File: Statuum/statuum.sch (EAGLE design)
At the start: 73 parts, among them IC1 LM317MABT, J1 POWER_JACKPTH, J2 NRJ3HF-1, J3 RCJ-21XXMILL, Q1 2N5484, Q10 ZVN4306A, Q11 ZVN4306A, Q12 ZVN4306A, Q2 2N5484, Q3 ZVN4306A, Q4 ZVN4306A, Q5 ZVN4306A, Q6 ZVN4306A, Q7 2N5484, Q8 2N5484, Q9 ZVN4306A

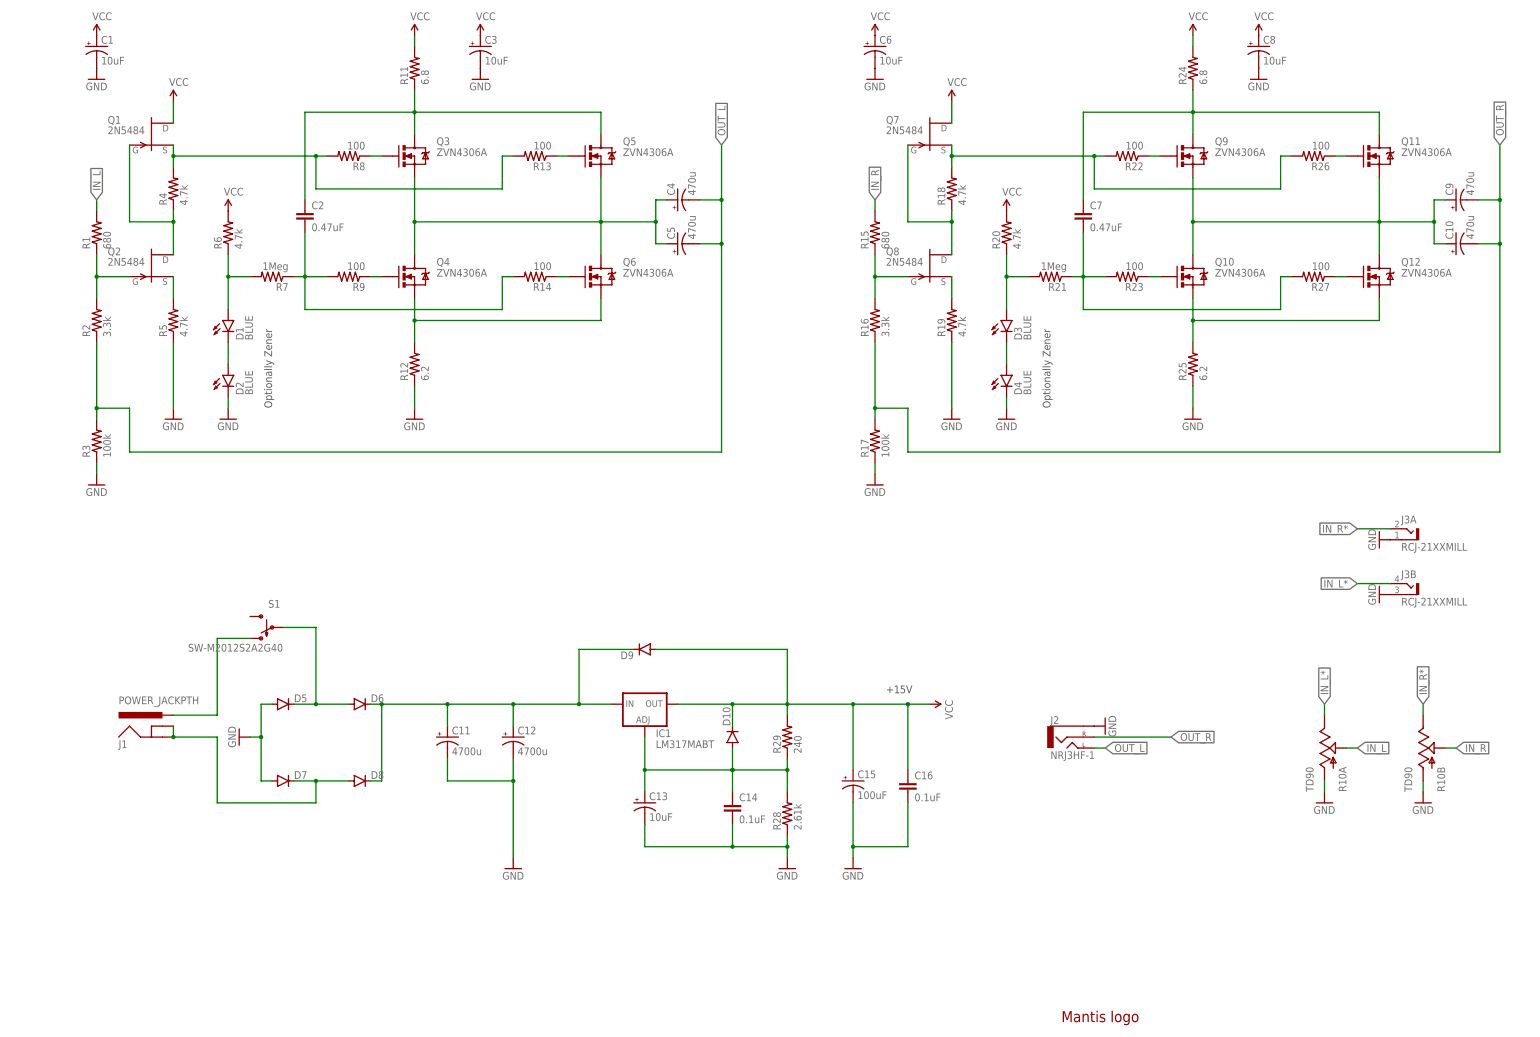
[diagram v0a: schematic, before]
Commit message: Desktop version changed to IRF510 output
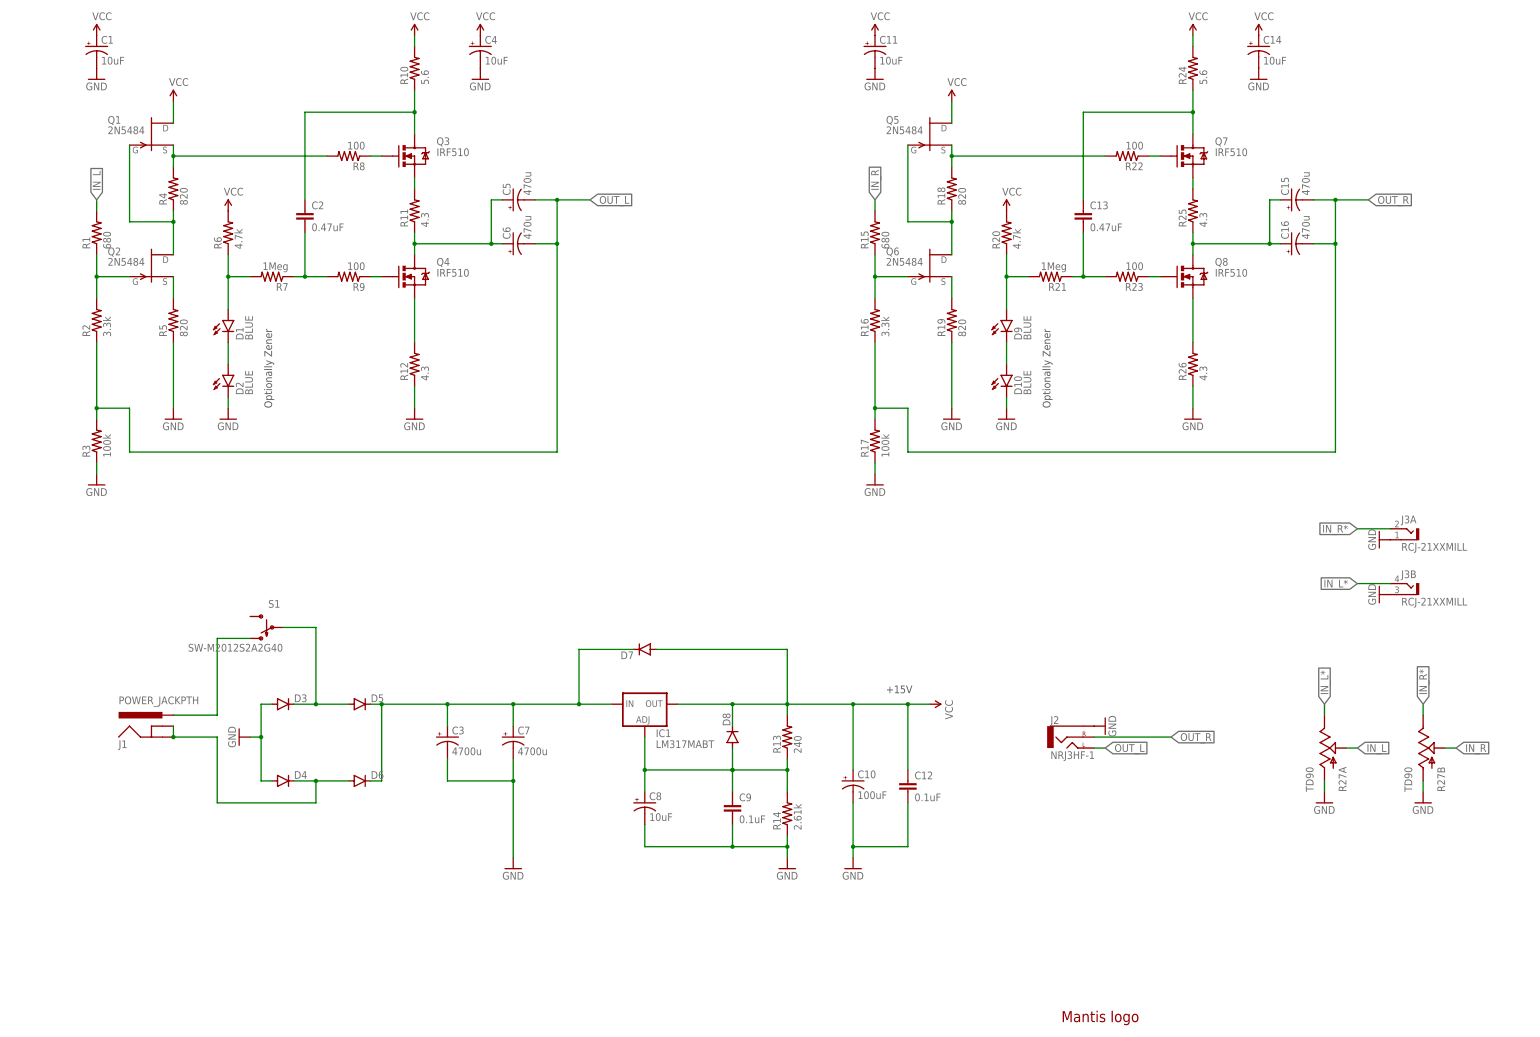
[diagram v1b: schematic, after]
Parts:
- removed Q10, Q11, Q12, Q9: ZVN4306A, my-tran:ZVN4306A
- removed R28: 2.61k, my-res:RESISTORPTH-1/4W
- removed R29: 240, my-res:RESISTORPTH-1/4W
- C10: value 470u -> 100uF
- C11: value 4700u -> 10uF; device SparkFun-Capacitors:CAP_POLPTH3 -> my-cap:CAP_POLPTH1-SM
- C12: value 4700u -> 0.1uF; device SparkFun-Capacitors:CAP_POLPTH3 -> SparkFun-Capacitors:CAPPTH
- C13: value 10uF -> 0.47uF; device my-cap:CAP_POLPTH1-SM -> capacitor-wima:C5/3.5
- C14: value 0.1uF -> 10uF; device SparkFun-Capacitors:CAPPTH -> my-cap:CAP_POLPTH1-SM
- C15: value 100uF -> 470u
- C16: value 0.1uF -> 470u; device SparkFun-Capacitors:CAPPTH -> my-cap:CAP_POLPTH8MM
- C3: value 10uF -> 4700u; device my-cap:CAP_POLPTH1-SM -> SparkFun-Capacitors:CAP_POLPTH3
- C4: value 470u -> 10uF; device my-cap:CAP_POLPTH8MM -> my-cap:CAP_POLPTH1-SM
- C6: value 10uF -> 470u; device my-cap:CAP_POLPTH1-SM -> my-cap:CAP_POLPTH8MM
- C7: value 0.47uF -> 4700u; device capacitor-wima:C5/3.5 -> SparkFun-Capacitors:CAP_POLPTH3
- C9: value 470u -> 0.1uF; device my-cap:CAP_POLPTH8MM -> SparkFun-Capacitors:CAPPTH
- D10, D9: value (none) -> BLUE; device SparkFun-DiscreteSemi:DIODEPTH -> my:LED3MM-SM
- D3, D4: value BLUE -> (none); device my:LED3MM-SM -> SparkFun-DiscreteSemi:DIODEPTH
- Q3, Q4: value ZVN4306A -> IRF510; device my-tran:ZVN4306A -> my-tran:IRF510
- Q5, Q6: value ZVN4306A -> 2N5484; device my-tran:ZVN4306A -> my-tran:2N5484
- Q7, Q8: value 2N5484 -> IRF510; device my-tran:2N5484 -> my-tran:IRF510
- R10: value TD90 -> 5.6; device my:TD90 -> my-res:RESISTORPTH-1/4W
- R11: value 6.8 -> 4.3
- R12, R25: value 6.2 -> 4.3
- R13: value 100 -> 240
- R14: value 100 -> 2.61k
- R18, R19, R4, R5: value 4.7k -> 820
- R24: value 6.8 -> 5.6
- R26: value 100 -> 4.3
- R27: value 100 -> TD90; device my-res:RESISTORPTH-1/4W -> my:TD90
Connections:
- removed net N$26: Q11.G, R26.1
- removed net N$27: Q12.G, R27.1
- net GND: now also C10.-, C12.2, C14.-, C4.-, C7.-, C9.2, D10.C, D3.A, D4.A, R14.1, R26.1, R27A.A, R27B.A; no longer C12.-, C13.-, C14.2, C15.-, C16.2, C6.-, D4.C, D5.A, D7.A, R10A.A, R10B.A, R25.1, R28.1
- net IN_L: now also R27A.S; no longer R10A.S
- net IN_L*: now also R27A.E; no longer R10A.E
- net IN_R: now also R27B.S; no longer R10B.S
- net IN_R*: now also R27B.E; no longer R10B.E
- net N$1: no longer R13.2
- net N$10: no longer Q6.S
- net N$11: now also R10.1; no longer Q5.D, R11.1
- net N$12: now also C6.+, R11.1; no longer C4.+, Q3.S, Q5.S, Q6.D
- net N$13: now also D3.C, D5.A; no longer D5.C, D6.A
- net N$15: no longer R14.2
- net N$16: now also Q5.S; no longer Q7.S, R26.2
- net N$17: now also Q5.G, Q6.D; no longer Q7.G, Q8.D
- net N$18: now also Q6.S; no longer Q8.S
- net N$19: now also Q6.G; no longer Q8.G
- net N$20: now also Q7.G; no longer Q9.G
- net N$21: now also Q8.G; no longer Q10.G
- net N$22: now also Q8.S, R26.2; no longer Q10.S, Q12.S, R25.2
- net N$23: now also C13.1, Q7.D; no longer C7.1, Q11.D, Q9.D
- net N$24: now also D9.A; no longer D3.A
- net N$25: now also D10.A, D9.C; no longer D3.C, D4.A
- net N$28: now also C13.2; no longer C7.2, R27.2
- net N$29: now also C15.+, C16.+, Q8.D, R25.1; no longer C10.+, C9.+, Q10.D, Q11.S, Q12.D, Q9.S
- net N$30: now also D4.C, D6.A; no longer D7.C, D8.A
- net N$32: now also C8.+, C9.1, D8.A, R13.1, R14.2; no longer C13.+, C14.1, D10.A, R28.2, R29.1
- net N$33: now also C3.+, C7.+, D5.C, D7.C; no longer C11.+, C12.+, D8.C, D9.C
- net N$7: now also Q3.S, R11.2; no longer Q5.G, R13.1
- net N$9: now also Q7.S, R25.2; no longer Q6.G, R14.1
- net OUT_L: now also C6.-; no longer C4.-
- net OUT_R: now also C15.-, C16.-; no longer C10.-, C9.-
- net VCC: now also C10.+, C11.+, C12.1, C14.+, C4.+, D7.A, D8.C, Q5.D, R10.2, R13.2; no longer C15.+, C16.1, C3.+, C6.+, C8.+, D10.C, D9.A, Q7.D, R11.2, R29.2
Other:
- moved on the sheet: C10, C11, C15, C3, C4, C5, C6, C8, D5, D6, D7, D8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

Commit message: Mounting holes
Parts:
- added H1: MOUNT-PAD-ROUND3.2, holes:MOUNT-PAD-ROUND3.2
- added H2: MOUNT-HOLE3.2, holes:MOUNT-HOLE3.2
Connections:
- net GND: now also H1.MOUNT
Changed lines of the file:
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@@
 <part name="Q8" library="my-tran" deviceset="IRF510" device=""/>
 <part name="R25" library="my-res" deviceset="RESISTOR" device="PTH-1/4W" value="4.3"/>
+<part name="H1" library="holes" deviceset="MOUNT-PAD-ROUND" device="3.2"/>
+<part name="H2" library="holes" deviceset="MOUNT-HOLE" device="3.2"/>
+<part name="GND22" library="SparkFun-Aesthetics" deviceset="GND" device=""/>
 </parts>
 <sheets>
@@
 <instance part="Q8" gate="G$1" x="287.02" y="180.34"/>
 <instance part="R25" gate="G$1" x="287.02" y="195.58" rot="R90"/>
+<instance part="H1" gate="G$1" x="294.64" y="35.56"/>
+<instance part="H2" gate="G$1" x="340.36" y="35.56"/>
+<instance part="GND22" gate="1" x="287.02" y="35.56" rot="R270"/>
 </instances>
 <busses>
@@
 <junction x="208.28" y="48.26"/>
 </segment>
-</net>
+<segment>
+<pinref part="H1" gate="G$1" pin="MOUNT"/>
+<wire x1="292.1" y1="35.56" x2="289.56" y2="35.56" width="0.1524" layer="91"/>
+<pinref part="GND22" gate="1" pin="GND"/>
+</segment>
+</net>

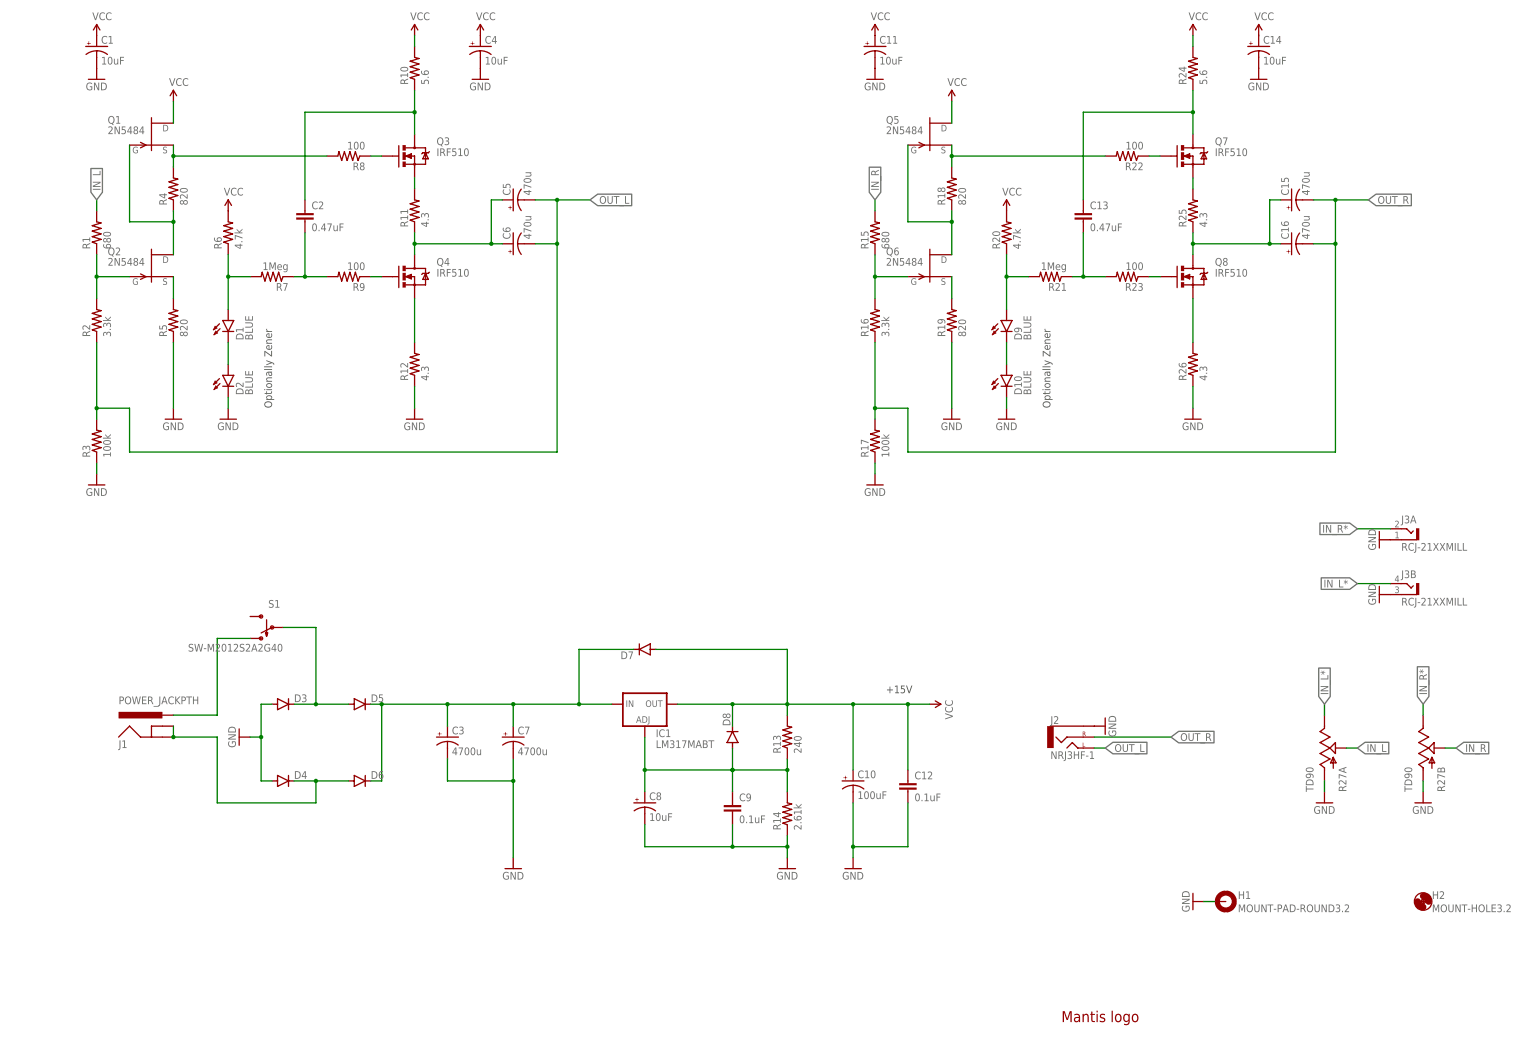
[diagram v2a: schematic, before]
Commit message: VBE multiplier added
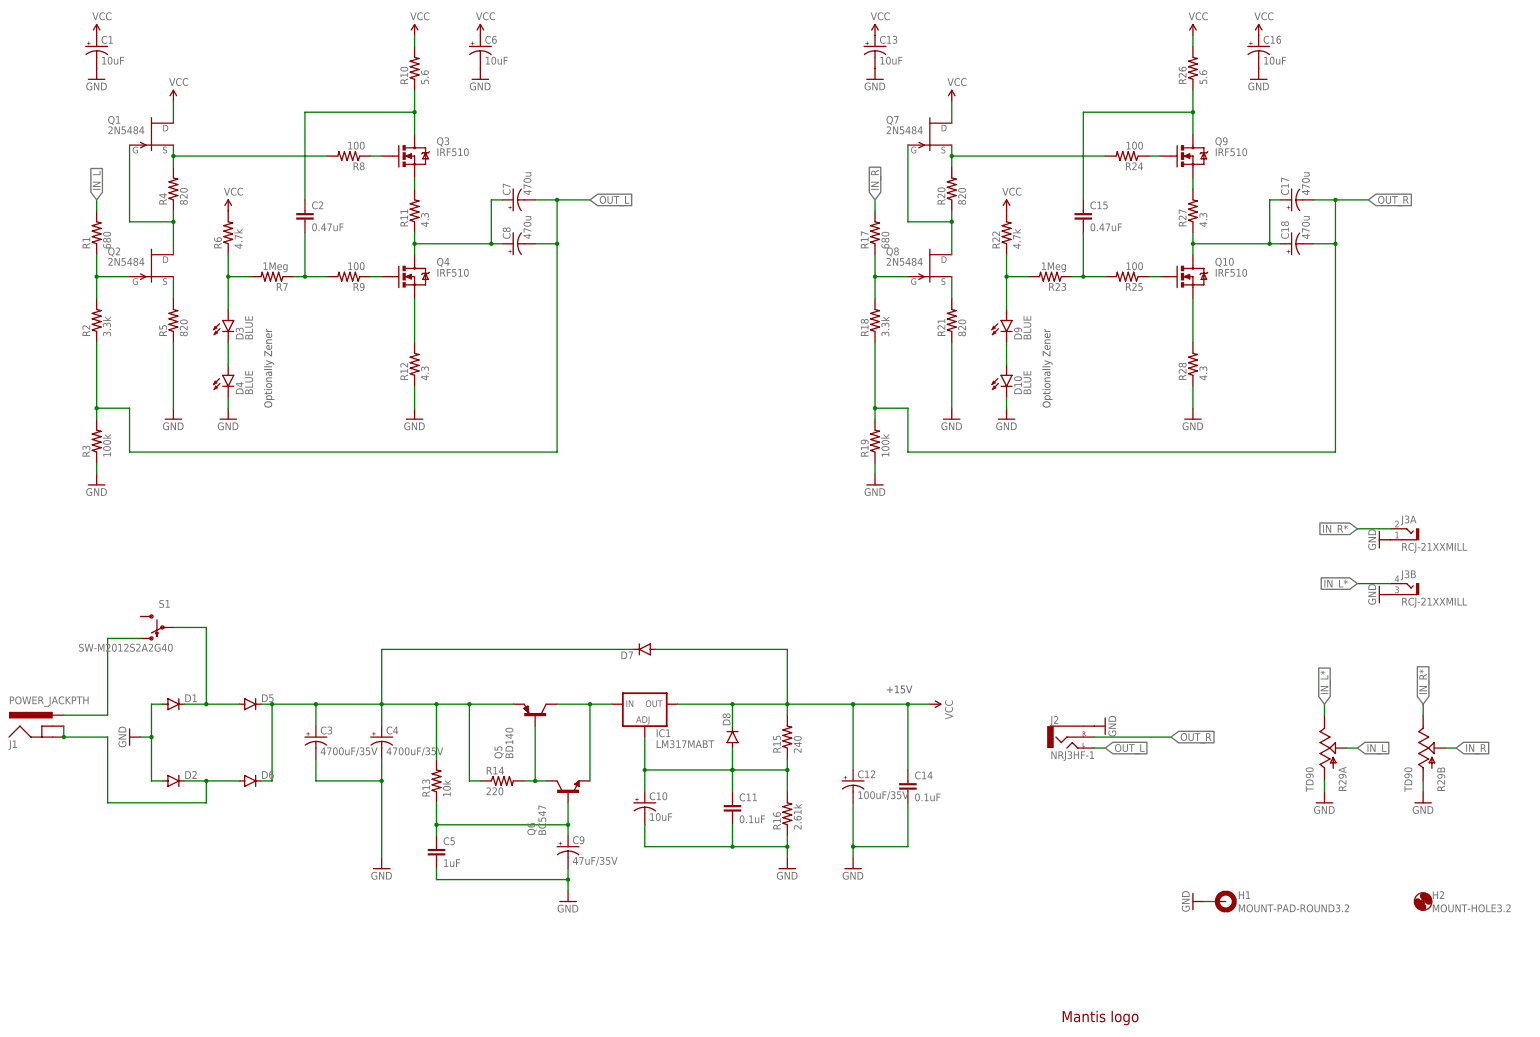
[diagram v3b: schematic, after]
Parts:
- added C17, C18: 470u, my-cap:CAP_POLPTH-8/3.5
- added Q10, Q9: IRF510, my-tran:IRF510
- added R28: 4.3, my-res:RESISTORPTH-1/4W
- added R29: TD90, my:TD90
- C1: device my-cap:CAP_POLPTH1-SM -> my-cap:CAP_POLPTH-5/2.5-SM
- C10: value 100uF -> 10uF; device my-cap:CAP_POLPTH8MM -> my-cap:CAP_POLPTH-5/2.5-SM
- C11, C14: value 10uF -> 0.1uF; device my-cap:CAP_POLPTH1-SM -> SparkFun-Capacitors:CAPPTH
- C12: value 0.1uF -> 100uF/35V; device SparkFun-Capacitors:CAPPTH -> my-cap:CAP_POLPTH-8/3.5
- C13: value 0.47uF -> 10uF; device capacitor-wima:C5/3.5 -> my-cap:CAP_POLPTH-5/2.5-SM
- C15: value 470u -> 0.47uF; device my-cap:CAP_POLPTH8MM -> capacitor-wima:C5/3.5
- C16, C6: value 470u -> 10uF; device my-cap:CAP_POLPTH8MM -> my-cap:CAP_POLPTH-5/2.5-SM
- C3: value 4700u -> 4700uF/35V
- C4: value 10uF -> 4700uF/35V; device my-cap:CAP_POLPTH1-SM -> my-cap:CAP_POLPTH-16/7.5
- C5: value 470u -> 1uF; device my-cap:CAP_POLPTH8MM -> SparkFun-Capacitors:CAPPTH
- C7: value 4700u -> 470u; device SparkFun-Capacitors:CAP_POLPTH3 -> my-cap:CAP_POLPTH-8/3.5
- C8: value 10uF -> 470u; device my-cap:CAP_POLPTH1-SM -> my-cap:CAP_POLPTH-8/3.5
- C9: value 0.1uF -> 47uF/35V; device SparkFun-Capacitors:CAPPTH -> my-cap:CAP_POLPTH-6.5/2.5
- D1, D2: value BLUE -> (none); device my:LED3MM-SM -> SparkFun-DiscreteSemi:DIODEPTH
- D3, D4: value (none) -> BLUE; device SparkFun-DiscreteSemi:DIODEPTH -> my:LED3MM-SM
- Q5: value 2N5484 -> BD140; device my-tran:2N5484 -> transistor-pnp:BD140
- Q6: value 2N5484 -> BC547; device my-tran:2N5484 -> my-tran:BC547
- Q7, Q8: value IRF510 -> 2N5484; device my-tran:IRF510 -> my-tran:2N5484
- R13: value 240 -> 10k
- R14: value 2.61k -> 220
- R15: value 680 -> 240
- R16: value 3.3k -> 2.61k
- R17: value 100k -> 680
- R18: value 820 -> 3.3k
- R19: value 820 -> 100k
- R20: value 4.7k -> 820
- R21: value 1Meg -> 820
- R22: value 100 -> 4.7k
- R23: value 100 -> 1Meg
- R24: value 5.6 -> 100
- R25: value 4.3 -> 100
- R26: value 4.3 -> 5.6
- R27: value TD90 -> 4.3; device my:TD90 -> my-res:RESISTORPTH-1/4W
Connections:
- removed net N$33: C3.+, C7.+, D5.C, D6.C, D7.C, IC1.IN
- new net N$26: Q5.B, Q6.C, R14.2
- new net N$27: C5.1, C9.+, Q6.B, R13.1
- new net N$34: C3.+, C4.+, D5.C, D6.C, D7.C, Q5.E, R13.2, R14.1
- new net N$36: IC1.IN, Q5.C, Q6.E
- net GND: now also C11.2, C12.-, C13.-, C14.2, C16.-, C5.2, C6.-, C9.-, D1.A, D2.A, D4.C, R16.1, R21.1, R28.1, R29A.A, R29B.A; no longer C11.-, C12.2, C14.-, C7.-, C8.-, C9.2, D2.C, D3.A, D4.A, R14.1, R17.1, R26.1, R27A.A, R27B.A
- net IN_L: now also R29A.S; no longer R27A.S
- net IN_L*: now also R29A.E; no longer R27A.E
- net IN_R: now also R17.2, R29B.S; no longer R15.2, R27B.S
- net IN_R*: now also R29B.E; no longer R27B.E
- net N$12: now also C7.+, C8.+; no longer C5.+, C6.+
- net N$13: now also D1.C; no longer D3.C
- net N$14: now also D3.A; no longer D1.A
- net N$16: now also Q7.S, R20.2, R24.2; no longer Q5.S, R18.2, R22.2
- net N$17: now also Q7.G, Q8.D, R20.1; no longer Q5.G, Q6.D, R18.1
- net N$18: now also Q8.S, R21.2; no longer Q6.S, R19.2
- net N$19: now also Q8.G, R17.1, R18.2; no longer Q6.G, R15.1, R16.2
- net N$20: now also Q9.G, R24.1; no longer Q7.G, R22.1
- net N$21: now also Q10.G, R25.1; no longer Q8.G, R23.1
- net N$22: now also Q10.S, R28.2; no longer Q8.S, R26.2
- net N$23: now also C15.1, Q9.D, R26.1; no longer C13.1, Q7.D, R24.1
- net N$24: now also R22.1, R23.2; no longer R20.1, R21.2
- net N$28: now also C15.2, R23.1, R25.2; no longer C13.2, R21.1, R23.2
- net N$29: now also C17.+, C18.+, Q10.D, R27.1; no longer C15.+, C16.+, Q8.D, R25.1
- net N$30: now also D2.C; no longer D4.C
- net N$32: now also C10.+, C11.1, R15.1, R16.2; no longer C8.+, C9.1, R13.1, R14.2
- net N$4: now also D3.C, D4.A; no longer D1.C, D2.A
- net N$9: now also Q9.S, R27.2; no longer Q7.S, R25.2
- net OUT_L: now also C7.-, C8.-; no longer C5.-, C6.-
- net OUT_R: now also C17.-, C18.-, R18.1, R19.2; no longer C15.-, C16.-, R16.1, R17.2
- net VCC: now also C12.+, C13.+, C14.1, C16.+, C6.+, Q7.D, R15.2, R22.2, R26.2; no longer C10.+, C11.+, C12.1, C14.+, C4.+, Q5.D, R13.2, R20.2, R24.2
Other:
- moved on the sheet: C10, C16, C3, C4, C6, C7, C8, D5, D6, J1, R13, R14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
